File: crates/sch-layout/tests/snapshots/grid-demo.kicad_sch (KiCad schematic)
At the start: 10 parts, among them U1 NE555P

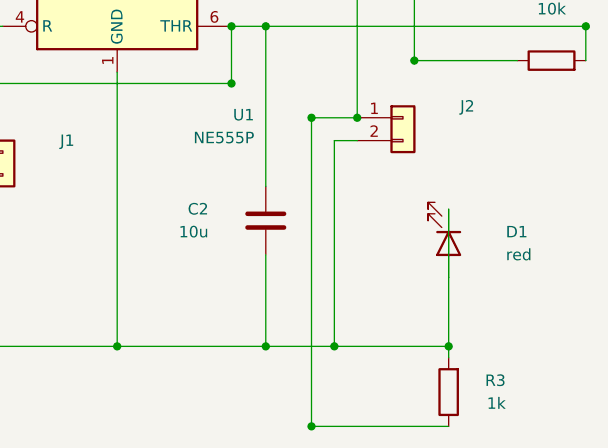
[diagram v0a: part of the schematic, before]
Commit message: fix(sch-engine): two realistic-board defects from the 20-circuit e2e sweep
A 20-board agent-generated sweep (all ERC-clean) surfaced two recurring
layout defects on realistic multi-module boards; both fixed here.

1. DECOUPLING BANK COLLAPSES ON ANY MULTI-IC BOARD. place_decoupling
   dropped every bypass cap whose net reached a SECOND IC — but a decoupling
   cap's two nets are BOTH rails (V+ and GND), and on every board with a
   regulator that V+ rail reaches the LDO as well as the MCU it bypasses. So
   the whole bank was ejected, fell below 3 caps, and scattered (the #1
   defect: c01/c02/c03). Fix: a shared RAIL never disqualifies a cap, only a
   shared SIGNAL net does. Deterministic repro idiom-stm32-ldo (kept as a
   fixture + idiom_detect regression test) goes 6 -> 8, bank restored.

2. RAIL TRUNK DRAWN THROUGH A STACKED CAP. When two same-rail caps land in
   one column, emit_rail drew the upper cap's riser straight down through the
   lower body (and a mis-oriented cap threads its own). emit_rail now jogs a
   blocked riser sideways out of the pin and descends in a clear lane
   (riser_hits_body + lane search), FINALIZE-ONLY (fan_risers) so the per-move
   scorer is untouched; crossing_counts now measures the shipped geometry.
   555 INFER 3 -> 0 crossings; grid-demo cleared a real one (snapshot
   re-blessed); the 4 reference targets stay byte-identical.

Gated: placement_snapshot + idiom_detect green, PREMIUM oracle
LAYOUT_SEARCH=anneal floorplan_netlist 2 passed (1170s).

Co-Authored-By: Claude Opus 4.8 (1M context) <noreply@anthropic.com>
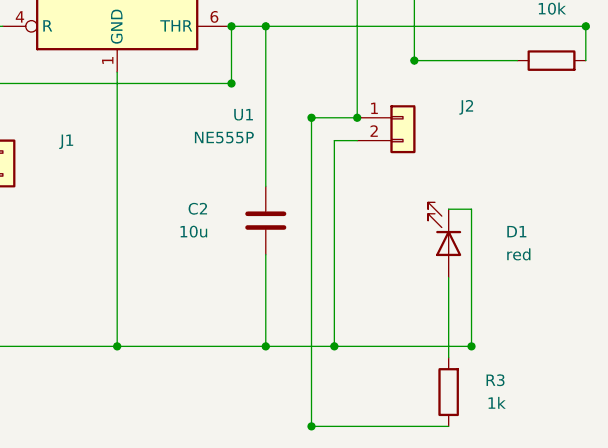
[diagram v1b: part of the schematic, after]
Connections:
- net GND: no longer D1.2 (A), R3.2
- new net: D1.2 (A), R3.2
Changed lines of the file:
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@@
 	(wire
 		(pts
-			(xy 77.47 80.01) (xy 90.17 80.01)
+			(xy 77.47 80.01) (xy 92.71 80.01)
 		)
 		(stroke (width 0) (type default))
@@
 	(wire
 		(pts
-			(xy 90.17 64.77) (xy 90.17 72.39)
+			(xy 90.17 64.77) (xy 92.71 64.77)
 		)
 		(stroke (width 0) (type default))
@@
 	(wire
 		(pts
-			(xy 90.17 72.39) (xy 90.17 80.01)
+			(xy 90.17 72.39) (xy 90.17 81.28)
 		)
 		(stroke (width 0) (type default))
@@
 	(wire
 		(pts
-			(xy 90.17 80.01) (xy 90.17 81.28)
+			(xy 92.71 64.77) (xy 92.71 80.01)
 		)
 		(stroke (width 0) (type default))
@@
 	)
 	(junction
-		(at 90.17 80.01)
+		(at 92.71 80.01)
 		(diameter 0)
 		(color 0 0 0 0)
